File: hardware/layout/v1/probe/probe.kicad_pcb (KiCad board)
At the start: 4 copper layers, 14 x 56 mm, 22 parts, among them J1 Main board, J2 Reflector T-Socket SMD, Q1 AO3400A, U1 SCD41-D-R2, U2 SGP41-D-R4, U3 SHT40-AD1F-R2, U4 LM2903DR2G, U5 BMP585

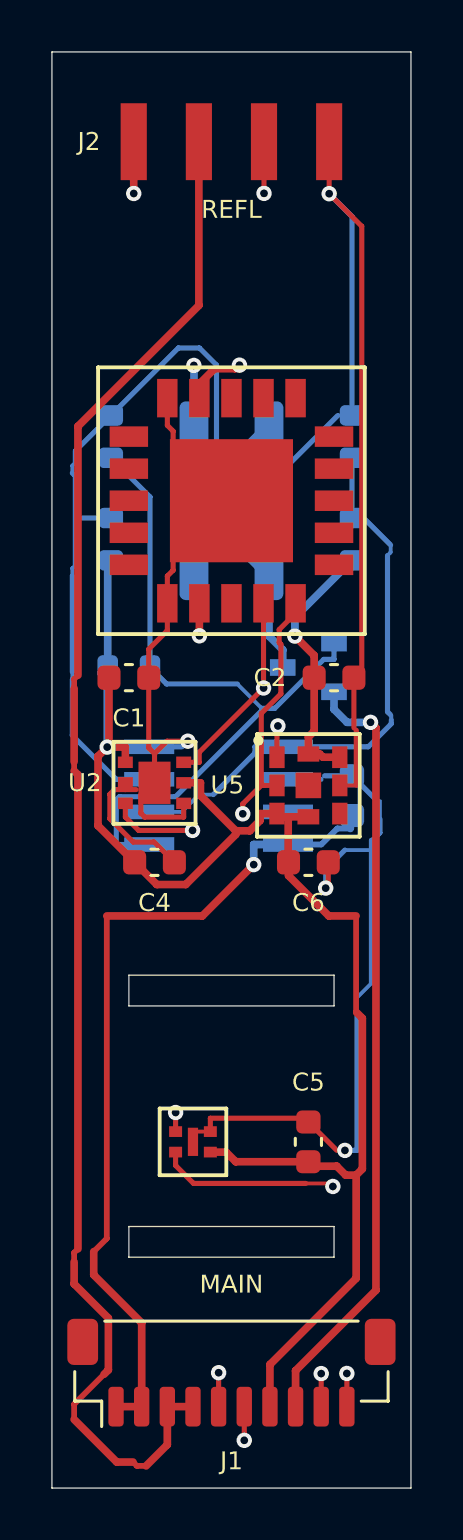
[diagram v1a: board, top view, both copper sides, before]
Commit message: Update dome PCB layout with manual reference and label placement, add Stock_Optional field for LTR-390UV-01 sensor to allow JLC assembly when in stock without failing release on shortage
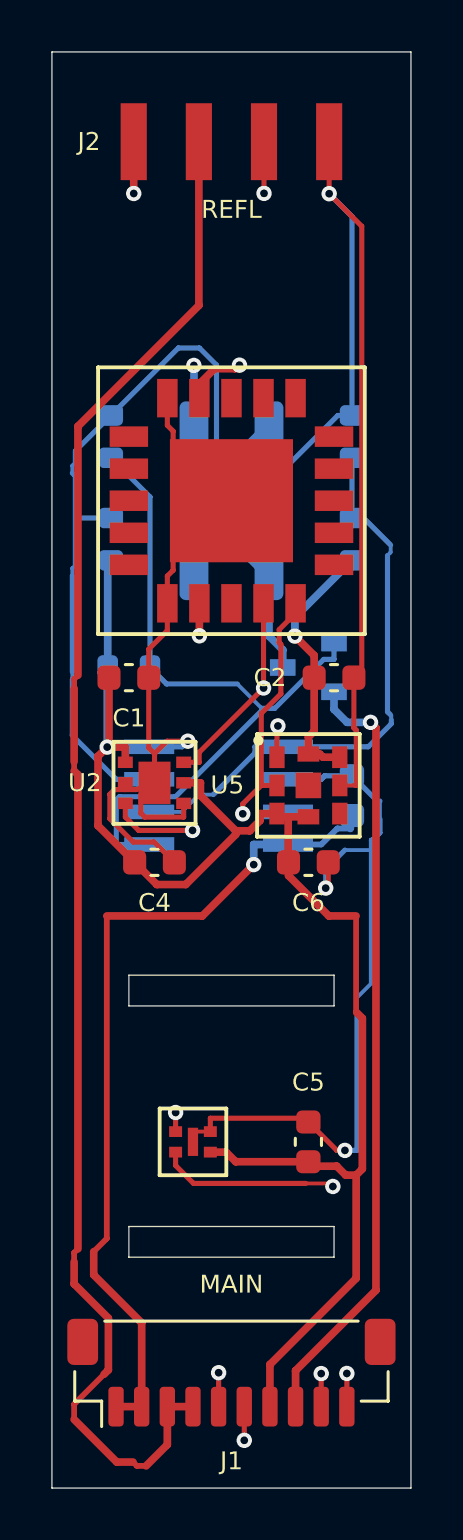
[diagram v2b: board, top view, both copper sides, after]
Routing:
- net GND: track 95.7 -> 98.7 mm
